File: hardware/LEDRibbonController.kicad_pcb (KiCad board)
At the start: 2 copper layers, 95.8 x 15.2 mm, 20 parts, among them J1 LED, J2 USB_OTG, J3 Battery, J4 ICSP, Q1 NTR4003NT1G, SW1 Mode, SW2 Power, U1 ATTINY10-TS, U2 MCP73831T-2ACI/OT

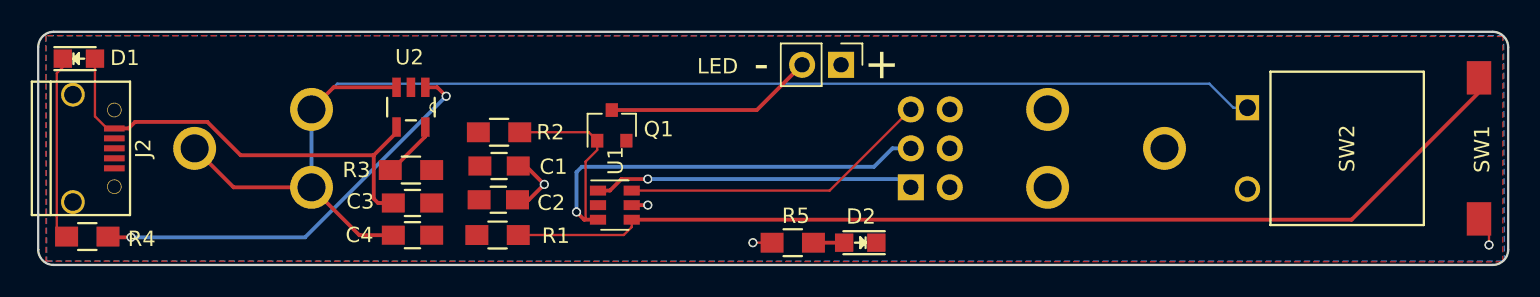
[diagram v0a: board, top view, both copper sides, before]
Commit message: Upgrade to kicad 5
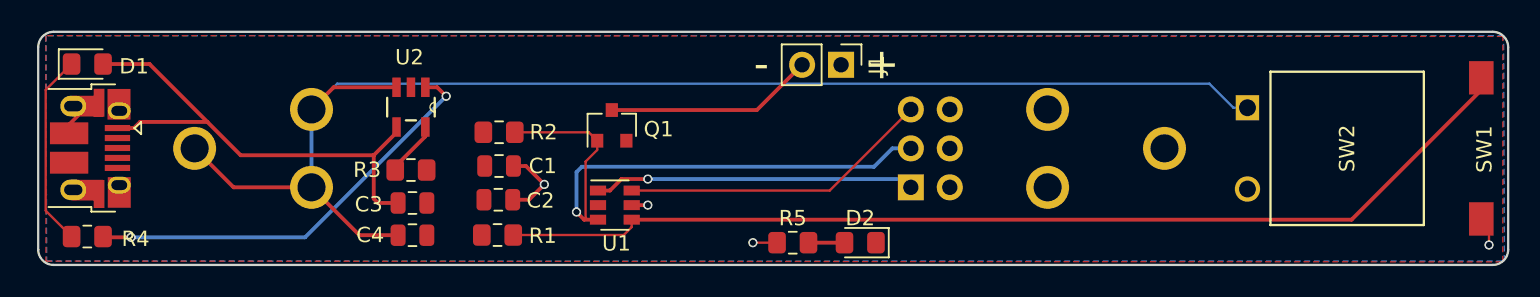
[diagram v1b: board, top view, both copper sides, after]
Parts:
- C1, C2, C3, C4: footprint Capacitors_SMD:C_0805_HandSoldering -> Capacitor_SMD:C_0805_2012Metric
- D1, D2: footprint LEDs:LED_0805 -> LED_SMD:LED_0805_2012Metric_Pad1.15x1.40mm_HandSolder
- J1: footprint Pin_Headers:Pin_Header_Straight_1x02_Pitch2.54mm -> Connector_PinHeader_2.54mm:PinHeader_1x02_P2.54mm_Vertical
- J2: value USB_OTG -> USB_B_Micro; footprint Jeremy:USB_Micro-B -> Connector_USB:USB_Micro-B_Amphenol_10103594-0001LF_Horizontal
- J4: footprint Pin_Headers:Pin_Header_Straight_2x03_Pitch2.54mm -> Connector_PinHeader_2.54mm:PinHeader_2x03_P2.54mm_Vertical
- Q1: footprint TO_SOT_Packages_SMD:SOT-23 -> Package_TO_SOT_SMD:SOT-23
- R1, R2, R3, R4: footprint Resistors_SMD:R_0805_HandSoldering -> Resistor_SMD:R_0805_2012Metric_Pad1.15x1.40mm_HandSolder
- R5: value 100 -> 470; footprint Resistors_SMD:R_0805_HandSoldering -> Resistor_SMD:R_0805_2012Metric_Pad1.15x1.40mm_HandSolder
- U1: value ATTINY10-TS -> ATtiny10-TS; footprint TO_SOT_Packages_SMD:SOT-23-6 -> Package_TO_SOT_SMD:SOT-23-6
- moved D1 0.65 mm to (100.7, 85.6)
- moved SW1 0.15 mm to (191.6, 91.1)
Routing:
- net Net-(C3-Pad1): track 30.2 -> 34.2 mm
- net GND: track 0.00 -> 2.27 mm

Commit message: Populate PCB with ALL THE NEW THINGS
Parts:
- added C5: 4.7uF, Capacitor_SMD:C_0603_1608Metric_Pad1.05x0.95mm_HandSolder, F.Cu at (118.2, 86.0)
- added C6: 4.7uF, Capacitor_SMD:C_0603_1608Metric_Pad1.05x0.95mm_HandSolder, F.Cu at (154.3, 90.6)
- added C7: 10uF, Capacitor_SMD:C_0603_1608Metric_Pad1.05x0.95mm_HandSolder, F.Cu at (125.8, 90.3)
- added C8: 22uF, Capacitor_SMD:C_0603_1608Metric_Pad1.05x0.95mm_HandSolder, F.Cu at (120.3, 94.5)
- added D3: 3v6, Diode_SMD:D_SOD-323, F.Cu at (101.4, 97.0)
- added D4: 3v6, Diode_SMD:D_SOD-323, F.Cu at (99.4, 97.0)
- added D5: 20V2A, Diode_SMD:D_SOD-323, F.Cu at (158.4, 87.2)
- added D6: 20V2A, Diode_SMD:D_SOD-323, F.Cu at (158.4, 85.2)
- added J5: Power, Connector_PinHeader_2.54mm:PinHeader_1x02_P2.54mm_Vertical, F.Cu at (128.6, 85.4)
- added L1: 2.2uH3A, Inductor_SMD:L_Vishay_IHLP-1212, F.Cu at (126.7, 96.7)
- added Q2: NTR4003NT1G, Package_TO_SOT_SMD:SOT-23, F.Cu at (146.6, 90.5)
- added Q3: NTR4003NT1G, Package_TO_SOT_SMD:SOT-23, F.Cu at (151.7, 90.5)
- added R10: 68, Resistor_SMD:R_0603_1608Metric_Pad1.05x0.95mm_HandSolder, F.Cu at (136.1, 86.3)
- added R12: 750K, Resistor_SMD:R_0603_1608Metric_Pad1.05x0.95mm_HandSolder, F.Cu at (120.4, 91.4)
- added R13: 100K, Resistor_SMD:R_0603_1608Metric_Pad1.05x0.95mm_HandSolder, F.Cu at (120.4, 92.9)
- added R6: 20k, Resistor_SMD:R_0603_1608Metric_Pad1.05x0.95mm_HandSolder, F.Cu at (151.6, 93.1)
- added R7: 2.2k, Resistor_SMD:R_0603_1608Metric_Pad1.05x0.95mm_HandSolder, F.Cu at (136.1, 84.8)
- added R8: 120, Resistor_SMD:R_0603_1608Metric_Pad1.05x0.95mm_HandSolder, F.Cu at (169.4, 97.5)
- added R9: 68, Resistor_SMD:R_0603_1608Metric_Pad1.05x0.95mm_HandSolder, F.Cu at (136.1, 87.9)
- added U3: PAM2401-8MSOP, Package_SO:MSOP-8_3x3mm_P0.65mm, F.Cu at (125.9, 93.0)
- C1: value 4.7uF -> 0.1uF; footprint Capacitor_SMD:C_0805_2012Metric -> Capacitor_SMD:C_0603_1608Metric_Pad1.05x0.95mm_HandSolder
- C2: value 0.1uF -> 4.7uF; footprint Capacitor_SMD:C_0805_2012Metric -> Capacitor_SMD:C_0603_1608Metric_Pad1.05x0.95mm_HandSolder
- C3, C4: footprint Capacitor_SMD:C_0805_2012Metric -> Capacitor_SMD:C_0603_1608Metric_Pad1.05x0.95mm_HandSolder
- D1, D2: footprint LED_SMD:LED_0805_2012Metric_Pad1.15x1.40mm_HandSolder -> LED_SMD:LED_0603_1608Metric_Castellated
- J1: value LED -> PWM; footprint Connector_PinHeader_2.54mm:PinHeader_1x02_P2.54mm_Vertical -> Connector_PinHeader_2.54mm:PinHeader_1x04_P2.54mm_Vertical
- J4: value ICSP -> ISP
- R1, R2, R3: footprint Resistor_SMD:R_0805_2012Metric_Pad1.15x1.40mm_HandSolder -> Resistor_SMD:R_0603_1608Metric_Pad1.05x0.95mm_HandSolder
- R4: value 470 -> 20k; footprint Resistor_SMD:R_0805_2012Metric_Pad1.15x1.40mm_HandSolder -> Resistor_SMD:R_0603_1608Metric_Pad1.05x0.95mm_HandSolder
- R5: footprint Resistor_SMD:R_0805_2012Metric_Pad1.15x1.40mm_HandSolder -> Resistor_SMD:R_0603_1608Metric
- U1: value ATtiny10-TS -> ATtiny85-20SU; footprint Package_TO_SOT_SMD:SOT-23-6 -> Package_SO:SOIC-8_3.9x4.9mm_P1.27mm
- moved R5 48.1 mm to (100.3, 84.5)
- moved R4 45.9 mm to (146.5, 93.1), turned to 0 degrees
- moved C4 27.9 mm to (149.1, 90.6), turned to 90 degrees
- moved D2 21.8 mm to (172.9, 97.5)
- moved C2 16.9 mm to (143.9, 90.7), turned to 90 degrees
- moved R2 14.1 mm to (141.3, 93.1), turned to 0 degrees
- moved Q1 6.57 mm to (141.4, 90.5)
- moved R3 6.24 mm to (123.2, 86.4), turned to 90 degrees
- moved C3 5.38 mm to (120.5, 89.5)
- moved R1 5.34 mm to (132.5, 95.1), turned to 270 degrees
- moved C1 5.14 mm to (132.5, 90.9), turned to 270 degrees
- moved J4 3.70 mm to (157.1, 96.2)
- moved J1 3.11 mm to (146.7, 85.8), turned to 90 degrees
- moved U2 2.29 mm to (120.6, 86.5)
- moved U1 2.05 mm to (136.0, 93.0), turned to 90 degrees
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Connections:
- net Net-(C3-Pad1) renamed Vin
- C1 pad 1: VCC -> +5V
- C2 pad 1: VCC -> GND
- C2 pad 2: GND -> VCC
- C4 pad 1: BATTERY -> GND
- C4 pad 2: GND -> VCC
- J1 pad 1: VCC -> +BATT
- J2 pad 4: Net-(J2-Pad4) -> (no net)
- J3 pad 1: BATTERY -> +BATT
- J4 pad 1: TPIDATA -> D-
- J4 pad 2: VCC -> +5V
- J4 pad 3: LED -> D+
- J4 pad 4: Net-(J4-Pad4) -> MOSI
- J4 pad 5: RESET -> RST
- Q1 pad 1: LED -> MOSI
- R2 pad 1: LED -> MOSI
- R4 pad 1: Net-(R4-Pad1) -> D-
- R4 pad 2: Net-(D1-Pad1) -> GND
- R5 pad 1: Net-(D2-Pad2) -> Net-(R5-Pad1)
- R5 pad 2: VCC -> Net-(D1-Pad1)
- SW1 pad 1: VCC -> +5V
- SW2 pad 1: BATTERY -> Net-(D5-Pad1)
- SW2 pad 2: VCC -> Net-(C7-Pad1)
- U1 pad 1: TPIDATA -> RST
- U1 pad 2: GND -> Net-(R1-Pad1)
- U1 pad 3: LED -> PWM3
- U1 pad 4: Net-(R1-Pad1) -> GND
- U1 pad 5: VCC -> MOSI
- U1 pad 6: RESET -> D-
- U2 pad 1: Net-(R4-Pad1) -> Net-(R5-Pad1)
- U2 pad 3: BATTERY -> +BATT
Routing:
- net BATTERY: track 88.9 -> 0.00 mm
- net Net-(C7-Pad1): track 0.00 -> 64.2 mm, vias 0 -> 1
- net +BATT: track 0.00 -> 51.2 mm
- net Net-(D4-Pad1): track 0.00 -> 47.4 mm, vias 0 -> 2
- net Net-(D3-Pad1): track 0.00 -> 41.7 mm, vias 0 -> 2
- net LED: track 38.1 -> 0.00 mm, vias 1 -> 0
- net Vin: track 34.2 -> 69.5 mm, vias 0 -> 4
- net D-: track 0.00 -> 30.8 mm, vias 0 -> 1
- net MOSI: track 0.00 -> 28.2 mm, vias 0 -> 1
- net Net-(R4-Pad1): track 27.5 -> 0.00 mm, vias 2 -> 0
- net D+: track 0.00 -> 26.9 mm, vias 0 -> 1
- net RST: track 0.00 -> 26.1 mm, vias 0 -> 2
- net Net-(R5-Pad1): track 0.00 -> 21.7 mm
- net TPIDATA: track 20.9 -> 0.00 mm, vias 1 -> 0
- net RESET: track 20.4 -> 0.00 mm
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- added copper zone on B.Cu, net +5V
- removed copper zone on B.Cu, net VCC
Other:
- net class Default: clearance 0.2 -> 0.1524; trace_width 0.25 -> 0.1524; via_dia 0.6 -> 0.6858; via_drill 0.4 -> 0.3302
- rule pad_to_mask_clearance: 0.2 -> 0.0508
- rule trace_clearance: 0.2 -> 0.1524
- rule trace_min: 0.154 -> 0.1524
- rule via_min_drill: 0.3 -> 0.3302
- rule via_min_size: 0.4 -> 0.6858
- board text added: "1"
- board text added: "2"
- board text added: "3"
- board text added: "BAT"
- board text added: "PWM"
- board text removed: "+"
- board text removed: "-"
- board text removed: "LED"

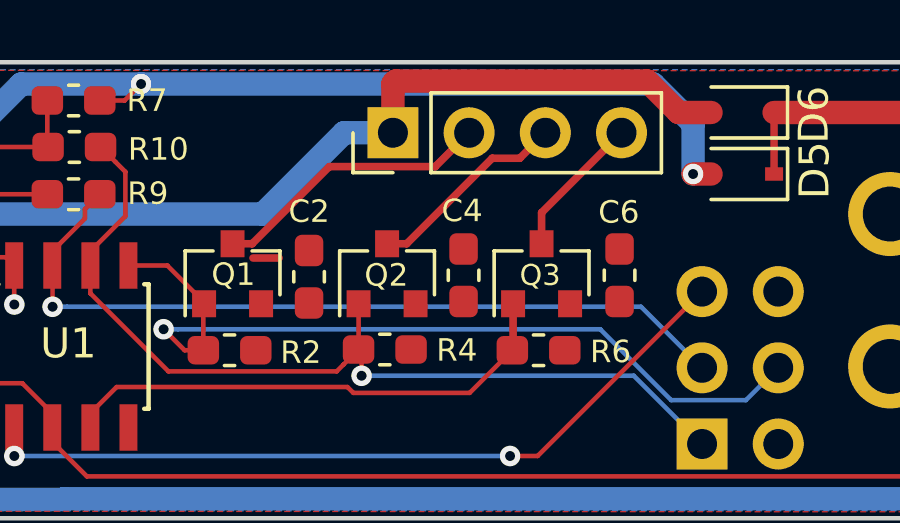
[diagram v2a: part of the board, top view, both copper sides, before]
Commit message: Remove VCC
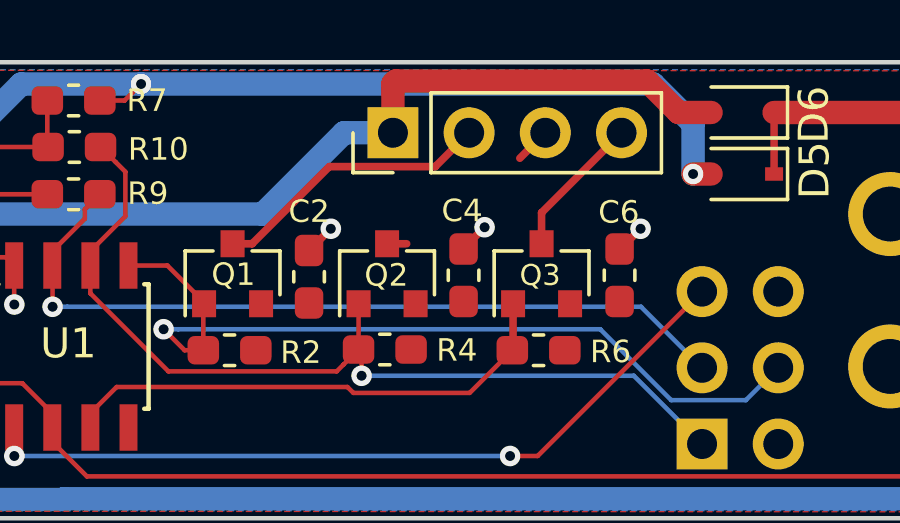
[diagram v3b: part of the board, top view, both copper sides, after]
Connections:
- C2 pad 2: VCC -> +5V
- C4 pad 2: VCC -> +5V
- C6 pad 2: VCC -> +5V
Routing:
- net Net-(J1-Pad3): track 6.81 -> 1.86 mm
- net +5V: track 9.46 -> 12.9 mm, vias 5 -> 8
- net (no net): track 0.87 -> 0.00 mm

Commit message: Finish routing
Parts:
- removed J5: Power, Connector_PinHeader_2.54mm:PinHeader_1x02_P2.54mm_Vertical
- added REF**: OSHW-Logo2_7.3x6mm_SilkScreen, Symbol:OSHW-Logo2_7.3x6mm_SilkScreen, B.Cu at (184.6, 95.1)
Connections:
- J1 pad 1: +BATT -> +5V
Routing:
- net +BATT: track 51.2 -> 63.9 mm, vias 0 -> 1
- net Net-(J1-Pad3): track 1.86 -> 6.81 mm
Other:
- board text added: "5v"
- board text added: "Blinky Fist rev2 Jeremy Gillick 2018"
- board text added: "Charge"
- board text added: "Power"
- board text removed: "BAT"
- board text removed: "Jeremy Gillick 2018"

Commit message: Adjust routing
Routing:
- net RST: track 26.1 -> 37.6 mm, vias 2 -> 1
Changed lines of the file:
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@@
     (thickness 1.6)
     (drawings 16)
-    (tracks 222)
+    (tracks 229)
     (zones 0)
     (modules 40)
@@
   )
   (setup
-    (last_trace_width 0.254)
+    (last_trace_width 0.154)
     (user_trace_width 0.154)
     (user_trace_width 0.254)
@@
   (segment (start 159.59 93.685) (end 158.511399 94.763601) (width 0.1524) (layer B.Cu) (net 14) (status 10))
   (segment (start 139.584933 92.4) (end 139.1 92.4) (width 0.1524) (layer B.Cu) (net 14))
-  (via (at 150.65 96.625) (size 0.6858) (drill 0.3302) (layers F.Cu B.Cu) (net 15))
-  (segment (start 151.57 96.625) (end 150.65 96.625) (width 0.154) (layer F.Cu) (net 15))
-  (segment (start 157.05 91.145) (end 151.57 96.625) (width 0.154) (layer F.Cu) (net 15) (status 10))
   (via (at 134.125 96.625) (size 0.6858) (drill 0.3302) (layers F.Cu B.Cu) (net 15))
-  (segment (start 150.65 96.625) (end 134.125 96.625) (width 0.154) (layer B.Cu) (net 15))
   (segment (start 134.125 95.68047) (end 134.120001 95.675471) (width 0.154) (layer F.Cu) (net 15) (status 30))
   (segment (start 134.125 96.625) (end 134.125 95.68047) (width 0.154) (layer F.Cu) (net 15) (status 20))
+  (segment (start 134.804401 97.304401) (end 134.125 96.625) (width 0.154) (layer B.Cu) (net 15))
+  (segment (start 158.083521 97.304401) (end 134.804401 97.304401) (width 0.154) (layer B.Cu) (net 15))
+  (segment (start 160.669401 94.203113) (end 159.726915 95.145599) (width 0.154) (layer B.Cu) (net 15))
+  (segment (start 160.669401 90.626887) (end 160.669401 94.203113) (width 0.154) (layer B.Cu) (net 15))
+  (segment (start 160.108113 90.065599) (end 160.669401 90.626887) (width 0.154) (layer B.Cu) (net 15))
+  (segment (start 158.129401 90.065599) (end 160.108113 90.065599) (width 0.154) (layer B.Cu) (net 15))
+  (segment (start 157.05 91.145) (end 158.129401 90.065599) (width 0.154) (layer B.Cu) (net 15))
+  (segment (start 159.726915 95.145599) (end 159.054401 95.145599) (width 0.154) (layer B.Cu) (net 15))
+  (segment (start 158.4 95.8) (end 158.4 96.987922) (width 0.154) (layer B.Cu) (net 15))
+  (segment (start 159.054401 95.145599) (end 158.4 95.8) (width 0.154) (layer B.Cu) (net 15))
+  (segment (start 158.4 96.987922) (end 158.083521 97.304401) (width 0.154) (layer B.Cu) (net 15))
   (segment (start 125.375 95.35) (end 125.375 96.7) (width 0.254) (layer F.Cu) (net 16) (status 20))
   (segment (start 126.775 93.95) (end 125.375 95.35) (width 0.254) (layer F.Cu) (net 16))
@@
   (segment (start 122.520041 85.500001) (end 119.460042 88.56) (width 0.781) (layer B.Cu) (net 22))
   (segment (start 143.725 85.5) (end 122.520041 85.500001) (width 0.781) (layer B.Cu) (net 22))
-  (segment (start 159.45 87.225) (end 159.45 85.175) (width 0.25) (layer F.Cu) (net 23) (status 30))
   (segment (start 176.35 88.387) (end 176.35 88.45) (width 0.781) (layer F.Cu) (net 23) (status 30))
   (segment (start 173.138 85.175) (end 176.35 88.387) (width 0.781) (layer F.Cu) (net 23) (status 20))
   (segment (start 159.45 85.175) (end 173.138 85.175) (width 0.781) (layer F.Cu) (net 23) (status 10))
+  (segment (start 159.45 87.225) (end 159.45 85.175) (width 0.781) (layer F.Cu) (net 23))
   (zone (net 7) (net_name +5V) (layer B.Cu) (hatch edge 0.508)
     (connect_pads (clearance 0.508))
